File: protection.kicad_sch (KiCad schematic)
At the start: 15 parts, among them Q1201 HL3400, U1201 LM74700

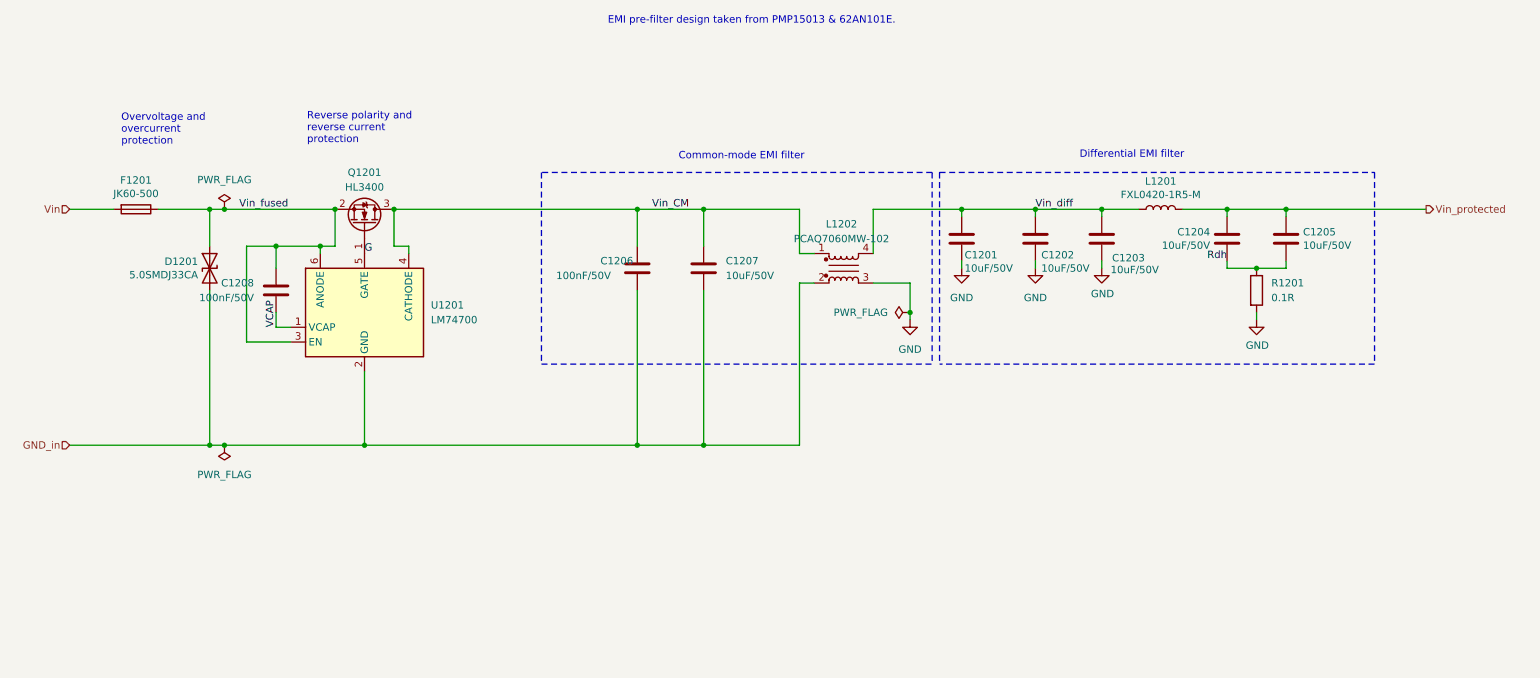
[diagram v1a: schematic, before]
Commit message: Reannotate components
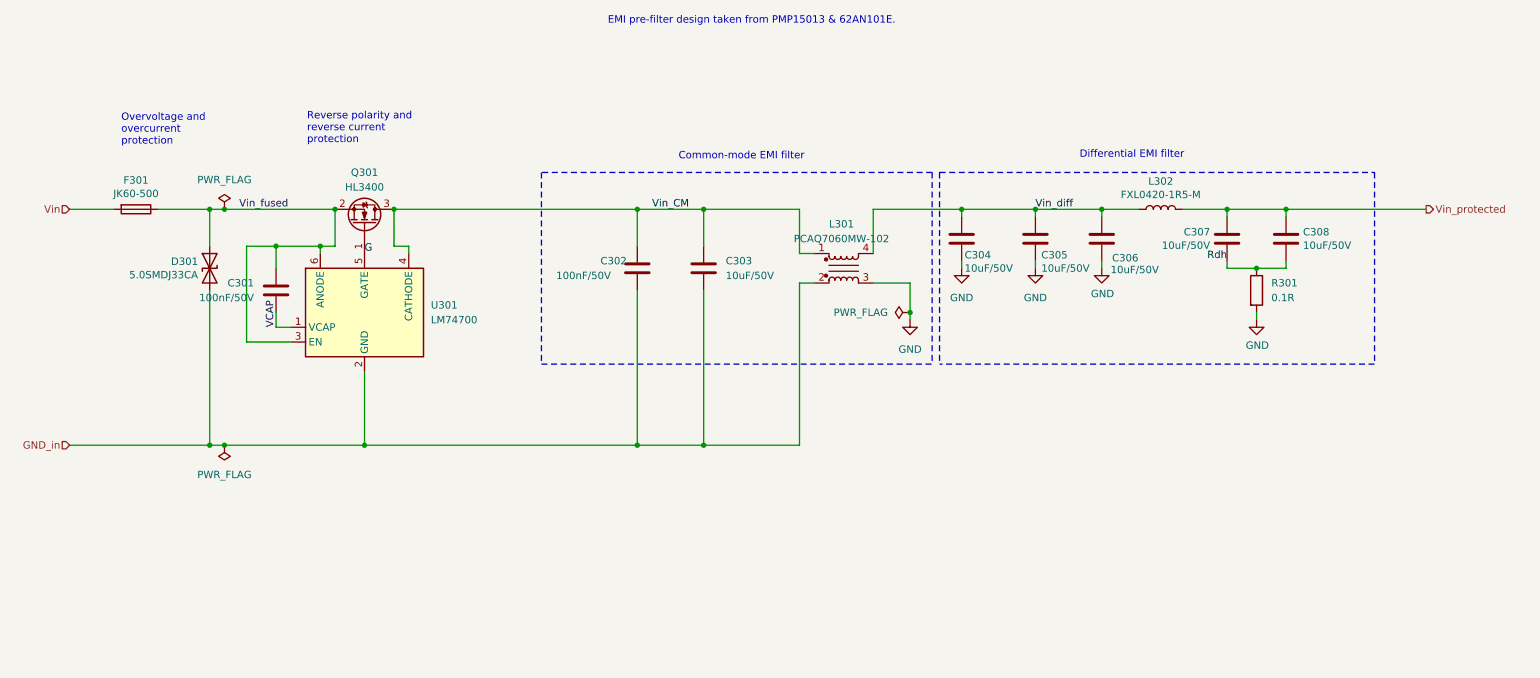
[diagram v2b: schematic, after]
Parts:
- renumbered C1208 to C301, C1206 to C302, C1207 to C303, C1201 to C304, C1202 to C305, C1203 to C306, C1204 to C307, C1205 to C308, D1201 to D301, F1201 to F301, L1202 to L301, L1201 to L302, Q1201 to Q301, R1201 to R301, U1201 to U301
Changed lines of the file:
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@@
 		(on_board yes)
 		(dnp no)
-		(property "Reference" "D1201"
+		(property "Reference" "D301"
 			(at 53.8734 62.3316 90)
 			(effects
@@
 			(project "SH-RPi"
 				(path "/abc482bd-3f17-4d35-80db-1da3dcdb5c27/c7bf4e1f-6bd1-4be7-9e56-1bd438bf5d42/b9ac802e-51d9-4be8-a7d3-5b5fa2c8bb97"
-					(reference "D1201")
+					(reference "D301")
 					(unit 1)
 				)
@@
 		(on_board yes)
 		(dnp no)
-		(property "Reference" "F1201"
+		(property "Reference" "F301"
 			(at 43.18 48.3362 90)
 			(effects
@@
 			(project "SH-RPi"
 				(path "/abc482bd-3f17-4d35-80db-1da3dcdb5c27/c7bf4e1f-6bd1-4be7-9e56-1bd438bf5d42/b9ac802e-51d9-4be8-a7d3-5b5fa2c8bb97"
-					(reference "F1201")
+					(reference "F301")
 					(unit 1)
 				)
@@
 		(on_board yes)
 		(dnp no)
-		(property "Reference" "C1203"
+		(property "Reference" "C306"
 			(at 211.328 61.722 0)
 			(effects
@@
 			(project "SH-RPi"
 				(path "/abc482bd-3f17-4d35-80db-1da3dcdb5c27/c7bf4e1f-6bd1-4be7-9e56-1bd438bf5d42/b9ac802e-51d9-4be8-a7d3-5b5fa2c8bb97"
-					(reference "C1203")
+					(reference "C306")
 					(unit 1)
 				)
@@
 		(on_board yes)
 		(dnp no)
-		(property "Reference" "#PWR01203"
+		(property "Reference" "#PWR0304"
 			(at 209.55 69.85 0)
 			(effects
@@
 			(project "SH-RPi"
 				(path "/abc482bd-3f17-4d35-80db-1da3dcdb5c27/c7bf4e1f-6bd1-4be7-9e56-1bd438bf5d42/b9ac802e-51d9-4be8-a7d3-5b5fa2c8bb97"
-					(reference "#PWR01203")
+					(reference "#PWR0304")
 					(unit 1)
 				)
@@
 		(on_board yes)
 		(dnp no)
-		(property "Reference" "L1201"
+		(property "Reference" "L302"
 			(at 219.71 48.514 90)
 			(effects
@@
 			(project "SH-RPi"
 				(path "/abc482bd-3f17-4d35-80db-1da3dcdb5c27/c7bf4e1f-6bd1-4be7-9e56-1bd438bf5d42/b9ac802e-51d9-4be8-a7d3-5b5fa2c8bb97"
-					(reference "L1201")
+					(reference "L302")
 					(unit 1)
 				)
@@
 		(on_board yes)
 		(dnp no)
-		(property "Reference" "C1204"
+		(property "Reference" "C307"
 			(at 228.219 57.2516 0)
 			(effects
@@
 			(project "SH-RPi"
 				(path "/abc482bd-3f17-4d35-80db-1da3dcdb5c27/c7bf4e1f-6bd1-4be7-9e56-1bd438bf5d42/b9ac802e-51d9-4be8-a7d3-5b5fa2c8bb97"
-					(reference "C1204")
+					(reference "C307")
 					(unit 1)
 				)
@@
 		(on_board yes)
 		(dnp no)
-		(property "Reference" "#PWR01205"
+		(property "Reference" "#PWR0305"
 			(at 236.22 78.74 0)
 			(effects
@@
 			(project "SH-RPi"
 				(path "/abc482bd-3f17-4d35-80db-1da3dcdb5c27/c7bf4e1f-6bd1-4be7-9e56-1bd438bf5d42/b9ac802e-51d9-4be8-a7d3-5b5fa2c8bb97"
-					(reference "#PWR01205")
+					(reference "#PWR0305")
 					(unit 1)
 				)
@@
 		(dnp no)
 		(fields_autoplaced yes)
-		(property "Reference" "#PWR01204"
+		(property "Reference" "#PWR0301"
 			(at 176.53 78.74 0)
 			(effects
@@
 			(project "SH-RPi"
 				(path "/abc482bd-3f17-4d35-80db-1da3dcdb5c27/c7bf4e1f-6bd1-4be7-9e56-1bd438bf5d42/b9ac802e-51d9-4be8-a7d3-5b5fa2c8bb97"
-					(reference "#PWR01204")
+					(reference "#PWR0301")
 					(unit 1)
 				)
@@
 		(dnp no)
 		(fields_autoplaced yes)
-		(property "Reference" "R1201"
+		(property "Reference" "R301"
 			(at 238.76 66.0399 0)
 			(effects
@@
 			(project "SH-RPi"
 				(path "/abc482bd-3f17-4d35-80db-1da3dcdb5c27/c7bf4e1f-6bd1-4be7-9e56-1bd438bf5d42/b9ac802e-51d9-4be8-a7d3-5b5fa2c8bb97"
-					(reference "R1201")
+					(reference "R301")
 					(unit 1)
 				)
@@
 		(on_board yes)
 		(dnp no)
-		(property "Reference" "C1205"
+		(property "Reference" "C308"
 			(at 244.221 57.2516 0)
 			(effects
@@
 			(project "Yellow"
 				(path "/abc482bd-3f17-4d35-80db-1da3dcdb5c27/c7bf4e1f-6bd1-4be7-9e56-1bd438bf5d42/b9ac802e-51d9-4be8-a7d3-5b5fa2c8bb97"
-					(reference "C1205")
+					(reference "C308")
 					(unit 1)
 				)
@@
 		(dnp no)
 		(fields_autoplaced yes)
-		(property "Reference" "#FLG01203"
+		(property "Reference" "#FLG0302"
 			(at 58.42 95.885 0)
 			(effects
@@
 			(project "SH-RPi"
 				(path "/abc482bd-3f17-4d35-80db-1da3dcdb5c27/c7bf4e1f-6bd1-4be7-9e56-1bd438bf5d42/b9ac802e-51d9-4be8-a7d3-5b5fa2c8bb97"
-					(reference "#FLG01203")
+					(reference "#FLG0302")
 					(unit 1)
 				)
@@
 		(dnp no)
 		(fields_autoplaced yes)
-		(property "Reference" "C1207"
+		(property "Reference" "C303"
 			(at 144.78 62.2299 0)
 			(effects
@@
 			(project "SH-RPi"
 				(path "/abc482bd-3f17-4d35-80db-1da3dcdb5c27/c7bf4e1f-6bd1-4be7-9e56-1bd438bf5d42/b9ac802e-51d9-4be8-a7d3-5b5fa2c8bb97"
-					(reference "C1207")
+					(reference "C303")
 					(unit 1)
 				)
@@
 		(on_board yes)
 		(dnp no)
-		(property "Reference" "C1201"
+		(property "Reference" "C304"
 			(at 185.928 61.214 0)
 			(effects
@@
 			(project "Yellow"
 				(path "/abc482bd-3f17-4d35-80db-1da3dcdb5c27/c7bf4e1f-6bd1-4be7-9e56-1bd438bf5d42/b9ac802e-51d9-4be8-a7d3-5b5fa2c8bb97"
-					(reference "C1201")
+					(reference "C304")
 					(unit 1)
 				)
@@
 		(on_board yes)
 		(dnp no)
-		(property "Reference" "C1202"
+		(property "Reference" "C305"
 			(at 199.136 61.214 0)
 			(effects
@@
 			(project "SH-RPi"
 				(path "/abc482bd-3f17-4d35-80db-1da3dcdb5c27/c7bf4e1f-6bd1-4be7-9e56-1bd438bf5d42/b9ac802e-51d9-4be8-a7d3-5b5fa2c8bb97"
-					(reference "C1202")
+					(reference "C305")
 					(unit 1)
 				)
@@
 		(on_board yes)
 		(dnp no)
-		(property "Reference" "C1206"
+		(property "Reference" "C302"
 			(at 123.19 62.23 0)
 			(effects
@@
 			(project "SH-RPi"
 				(path "/abc482bd-3f17-4d35-80db-1da3dcdb5c27/c7bf4e1f-6bd1-4be7-9e56-1bd438bf5d42/b9ac802e-51d9-4be8-a7d3-5b5fa2c8bb97"
-					(reference "C1206")
+					(reference "C302")
 					(unit 1)
 				)
@@
 		(dnp no)
 		(fields_autoplaced yes)
-		(property "Reference" "#PWR01201"
+		(property "Reference" "#PWR0302"
 			(at 185.42 69.85 0)
 			(effects
@@
 			(project "Yellow"
 				(path "/abc482bd-3f17-4d35-80db-1da3dcdb5c27/c7bf4e1f-6bd1-4be7-9e56-1bd438bf5d42/b9ac802e-51d9-4be8-a7d3-5b5fa2c8bb97"
-					(reference "#PWR01201")
+					(reference "#PWR0302")
 					(unit 1)
 				)
@@
 		(dnp no)
 		(fields_autoplaced yes)
-		(property "Reference" "U1201"
+		(property "Reference" "U301"
 			(at 93.98 69.8499 0)
 			(effects
@@
 			(project "HALPI2"
 				(path "/abc482bd-3f17-4d35-80db-1da3dcdb5c27/c7bf4e1f-6bd1-4be7-9e56-1bd438bf5d42/b9ac802e-51d9-4be8-a7d3-5b5fa2c8bb97"
-					(reference "U1201")
+					(reference "U301")
 					(unit 1)
 				)
@@
 		(dnp no)
 		(fields_autoplaced yes)
-		(property "Reference" "#FLG01201"
+		(property "Reference" "#FLG0301"
 			(at 58.42 51.435 0)
 			(effects
@@
 			(project "HALPI2"
 				(path "/abc482bd-3f17-4d35-80db-1da3dcdb5c27/c7bf4e1f-6bd1-4be7-9e56-1bd438bf5d42/b9ac802e-51d9-4be8-a7d3-5b5fa2c8bb97"
-					(reference "#FLG01201")
+					(reference "#FLG0301")
 					(unit 1)
 				)
@@
 		(dnp no)
 		(fields_autoplaced yes)
-		(property "Reference" "L1202"
+		(property "Reference" "L301"
 			(at 164.719 55.88 0)
 			(effects
@@
 			(project "SH-RPi"
 				(path "/abc482bd-3f17-4d35-80db-1da3dcdb5c27/c7bf4e1f-6bd1-4be7-9e56-1bd438bf5d42/b9ac802e-51d9-4be8-a7d3-5b5fa2c8bb97"
-					(reference "L1202")
+					(reference "L301")
 					(unit 1)
 				)
@@
 		(dnp no)
 		(fields_autoplaced yes)
-		(property "Reference" "Q1201"
+		(property "Reference" "Q301"
 			(at 82.55 46.99 90)
 			(effects
@@
 			(project ""
 				(path "/abc482bd-3f17-4d35-80db-1da3dcdb5c27/c7bf4e1f-6bd1-4be7-9e56-1bd438bf5d42/b9ac802e-51d9-4be8-a7d3-5b5fa2c8bb97"
-					(reference "Q1201")
+					(reference "Q301")
 					(unit 1)
 				)
@@
 		(dnp no)
 		(fields_autoplaced yes)
-		(property "Reference" "#FLG01202"
+		(property "Reference" "#FLG0303"
 			(at 174.625 71.12 0)
 			(effects
@@
 			(project "HALPI2"
 				(path "/abc482bd-3f17-4d35-80db-1da3dcdb5c27/c7bf4e1f-6bd1-4be7-9e56-1bd438bf5d42/b9ac802e-51d9-4be8-a7d3-5b5fa2c8bb97"
-					(reference "#FLG01202")
+					(reference "#FLG0303")
 					(unit 1)
 				)
@@
 		(dnp no)
 		(fields_autoplaced yes)
-		(property "Reference" "#PWR01202"
+		(property "Reference" "#PWR0303"
 			(at 198.12 69.85 0)
 			(effects
@@
 			(project "SH-RPi"
 				(path "/abc482bd-3f17-4d35-80db-1da3dcdb5c27/c7bf4e1f-6bd1-4be7-9e56-1bd438bf5d42/b9ac802e-51d9-4be8-a7d3-5b5fa2c8bb97"
-					(reference "#PWR01202")
+					(reference "#PWR0303")
 					(unit 1)
 				)
@@
 		(on_board yes)
 		(dnp no)
-		(property "Reference" "C1208"
+		(property "Reference" "C301"
 			(at 63.5 66.0399 0)
 			(effects
@@
 			(project "HALPI2"
 				(path "/abc482bd-3f17-4d35-80db-1da3dcdb5c27/c7bf4e1f-6bd1-4be7-9e56-1bd438bf5d42/b9ac802e-51d9-4be8-a7d3-5b5fa2c8bb97"
-					(reference "C1208")
-					(unit 1)
-				)
+					(reference "C301")
+					(unit 1)
+				)

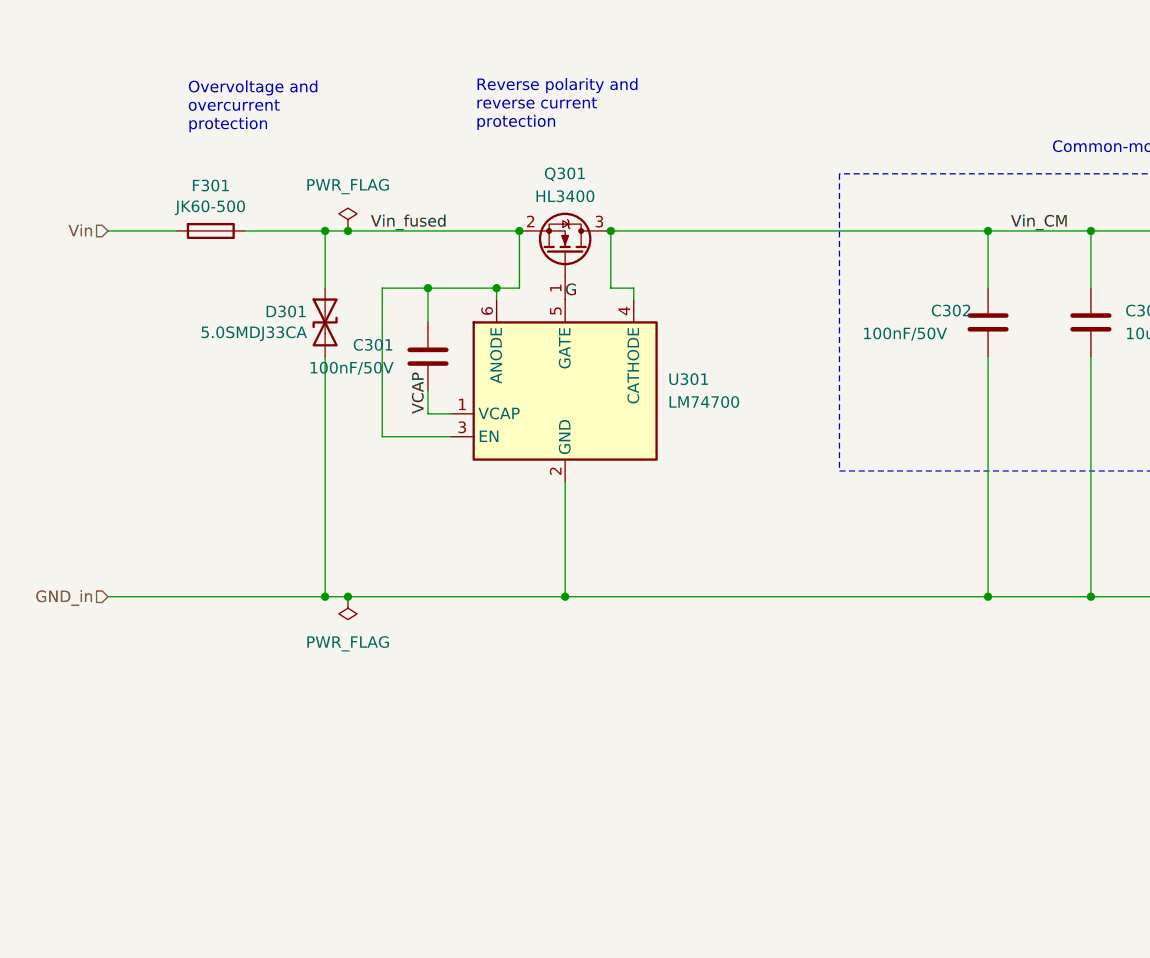
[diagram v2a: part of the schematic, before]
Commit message: Most DRC errors fixed
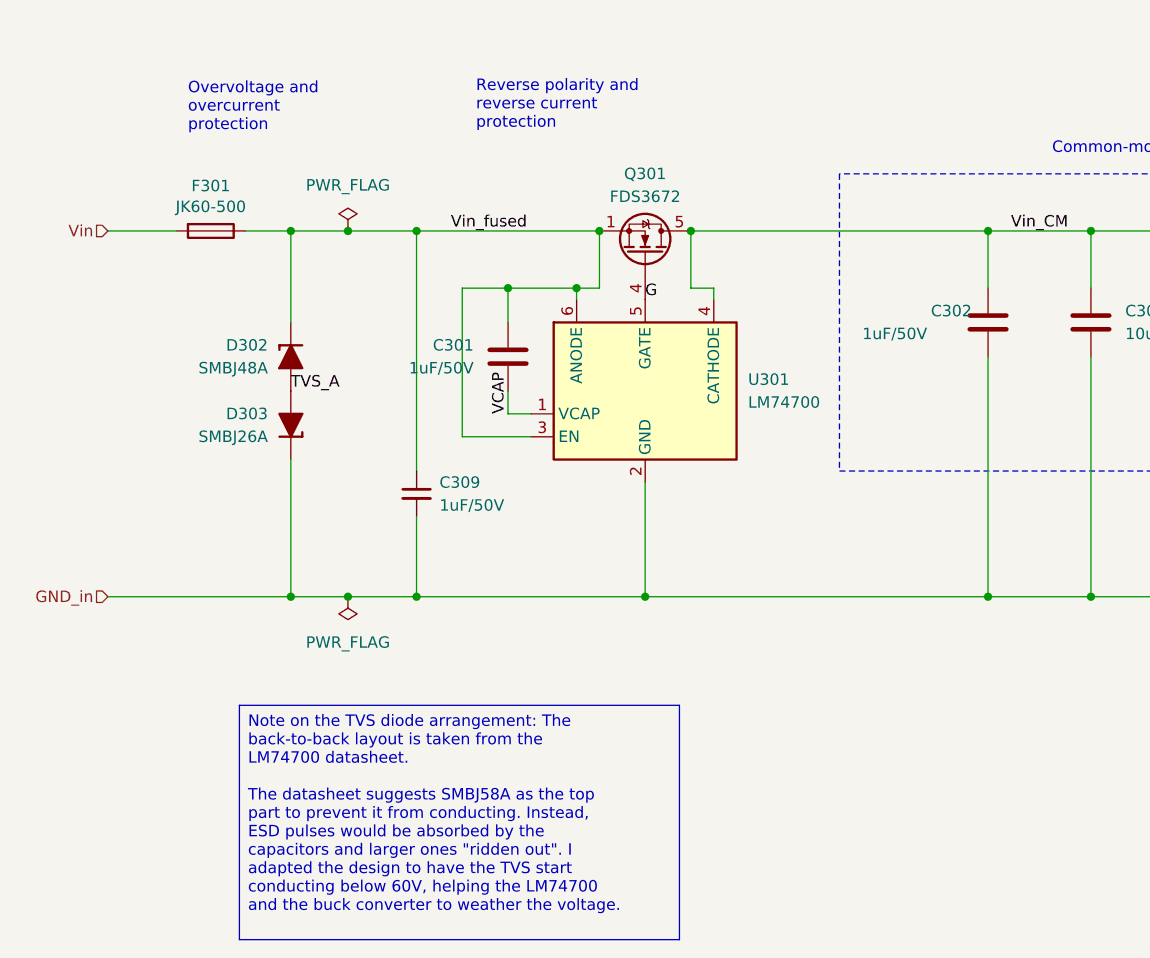
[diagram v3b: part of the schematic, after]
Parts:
- removed D301: 5.0SMDJ33CA, Diode_SMD:D_SMC, symbol Device:D_TVS
- added C309: 1uF/50V, Capacitor_SMD:C_1206_3216Metric, symbol Device:C_Small
- added D302: SMBJ48A, PCM_Diode_SMD_AKL:D_SMB, symbol PCM_Diode_TVS_AKL:SMBJ58A
- added D303: SMBJ26A, PCM_Diode_SMD_AKL:D_SMB, symbol PCM_Diode_TVS_AKL:SMBJ26A
- C301, C302: value 100nF/50V -> 1uF/50V; LCSC C14663 -> C15849
- L301: footprint Hatlabs:L_CMF7060F -> Hatlabs:FILTER-SMD_4P-L7.0-W6.0-TL-A
- Q301: value HL3400 -> FDS3672; footprint Package_TO_SOT_SMD:SOT-23 -> Package_SO:SOP-8_3.9x4.9mm_P1.27mm; symbol Hatlabs:HL3400 -> Hatlabs:FDS3672; LCSC C22469448 -> C5296734
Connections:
- net G: now also Q301.4 (G); no longer Q301.1 (G)
- net GND_in: now also C309.2, D303.1 (K)
- net Vin_CM: now also Q301.5 (D), Q301.6 (D), Q301.7 (D), Q301.8 (D); no longer Q301.3 (D)
- net Vin_fused: now also Q301.1 (S), Q301.3 (S), C309.1, D302.1 (K)
- new net TVS_A: D302.2 (A), D303.2 (A)
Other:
- moved on the sheet: C301, Q301, U301

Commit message: Fix most DRC errors, partial silk screen
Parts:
- D302, D303: footprint PCM_Diode_SMD_AKL:D_SMB -> Diode_SMD:D_SMB
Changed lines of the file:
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@@
 			)
 		)
-		(property "Footprint" "PCM_Diode_SMD_AKL:D_SMB"
+		(property "Footprint" "Diode_SMD:D_SMB"
 			(at 52.07 67.31 0)
 			(effects
@@
 			)
 		)
-		(property "Footprint" "PCM_Diode_SMD_AKL:D_SMB"
+		(property "Footprint" "Diode_SMD:D_SMB"
 			(at 52.07 74.93 0)
 			(effects
